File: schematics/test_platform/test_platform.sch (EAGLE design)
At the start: 13 parts

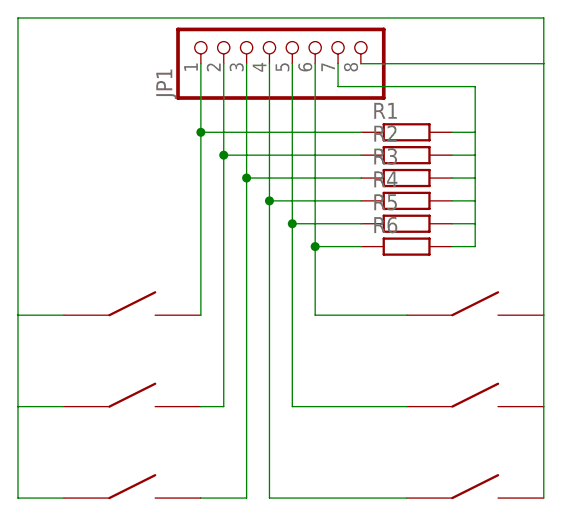
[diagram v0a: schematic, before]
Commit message: test platform ready for production, except for button footprints
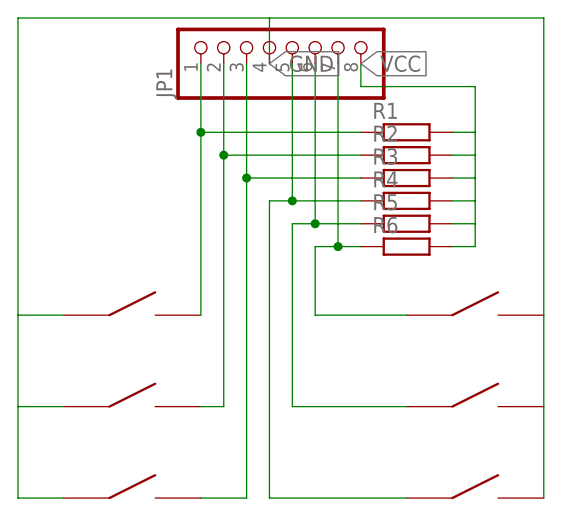
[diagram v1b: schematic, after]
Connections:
- removed net N$7: JP1.7, R1.2, R2.2, R3.2, R4.2, R5.2, R6.2
- removed net N$8: JP1.8, U$1.A, U$2.A, U$3.A, U$4.B, U$5.B, U$6.B
- new net GND: JP1.4, U$1.A, U$2.A, U$3.A, U$4.B, U$5.B, U$6.B
- new net VCC: JP1.8, R1.2, R2.2, R3.2, R4.2, R5.2, R6.2
- net N$4: now also JP1.5; no longer JP1.4
- net N$5: now also JP1.6; no longer JP1.5
- net N$6: now also JP1.7; no longer JP1.6
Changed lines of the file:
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@@
 <net name="N$4" class="0">
 <segment>
-<pinref part="JP1" gate="G$1" pin="4"/>
-<wire x1="73.66" y1="76.2" x2="73.66" y2="60.96" width="0.1524" layer="91"/>
 <pinref part="U$6" gate="G$1" pin="A"/>
 <wire x1="73.66" y1="60.96" x2="73.66" y2="27.94" width="0.1524" layer="91"/>
 <wire x1="73.66" y1="27.94" x2="88.9" y2="27.94" width="0.1524" layer="91"/>
 <pinref part="R4" gate="G$1" pin="1"/>
-<wire x1="73.66" y1="60.96" x2="83.82" y2="60.96" width="0.1524" layer="91"/>
-<junction x="73.66" y="60.96"/>
+<wire x1="73.66" y1="60.96" x2="76.2" y2="60.96" width="0.1524" layer="91"/>
+<pinref part="JP1" gate="G$1" pin="5"/>
+<wire x1="76.2" y1="60.96" x2="83.82" y2="60.96" width="0.1524" layer="91"/>
+<wire x1="76.2" y1="76.2" x2="76.2" y2="60.96" width="0.1524" layer="91"/>
+<junction x="76.2" y="60.96"/>
 </segment>
 </net>
@@
 <pinref part="U$5" gate="G$1" pin="A"/>
 <wire x1="88.9" y1="38.1" x2="76.2" y2="38.1" width="0.1524" layer="91"/>
-<pinref part="JP1" gate="G$1" pin="5"/>
 <wire x1="76.2" y1="38.1" x2="76.2" y2="58.42" width="0.1524" layer="91"/>
 <pinref part="R5" gate="G$1" pin="1"/>
-<wire x1="76.2" y1="58.42" x2="76.2" y2="76.2" width="0.1524" layer="91"/>
-<wire x1="83.82" y1="58.42" x2="76.2" y2="58.42" width="0.1524" layer="91"/>
-<junction x="76.2" y="58.42"/>
+<wire x1="83.82" y1="58.42" x2="78.74" y2="58.42" width="0.1524" layer="91"/>
+<pinref part="JP1" gate="G$1" pin="6"/>
+<wire x1="78.74" y1="58.42" x2="76.2" y2="58.42" width="0.1524" layer="91"/>
+<wire x1="78.74" y1="76.2" x2="78.74" y2="58.42" width="0.1524" layer="91"/>
+<junction x="78.74" y="58.42"/>
 </segment>
 </net>
 <net name="N$6" class="0">
 <segment>
-<pinref part="JP1" gate="G$1" pin="6"/>
-<wire x1="78.74" y1="76.2" x2="78.74" y2="55.88" width="0.1524" layer="91"/>
 <pinref part="U$4" gate="G$1" pin="A"/>
 <wire x1="78.74" y1="55.88" x2="78.74" y2="48.26" width="0.1524" layer="91"/>
 <wire x1="78.74" y1="48.26" x2="88.9" y2="48.26" width="0.1524" layer="91"/>
 <pinref part="R6" gate="G$1" pin="1"/>
-<wire x1="78.74" y1="55.88" x2="83.82" y2="55.88" width="0.1524" layer="91"/>
-<junction x="78.74" y="55.88"/>
+<wire x1="78.74" y1="55.88" x2="81.28" y2="55.88" width="0.1524" layer="91"/>
+<pinref part="JP1" gate="G$1" pin="7"/>
+<wire x1="81.28" y1="55.88" x2="83.82" y2="55.88" width="0.1524" layer="91"/>
+<wire x1="81.28" y1="76.2" x2="81.28" y2="55.88" width="0.1524" layer="91"/>
+<junction x="81.28" y="55.88"/>
 </segment>
 </net>
-<net name="N$8" class="0">
+<net name="GND" class="0">
 <segment>
 <pinref part="U$6" gate="G$1" pin="B"/>
@@
 <wire x1="104.14" y1="38.1" x2="104.14" y2="48.26" width="0.1524" layer="91"/>
 <pinref part="U$4" gate="G$1" pin="B"/>
-<wire x1="104.14" y1="48.26" x2="104.14" y2="76.2" width="0.1524" layer="91"/>
+<wire x1="104.14" y1="48.26" x2="104.14" y2="81.28" width="0.1524" layer="91"/>
 <pinref part="U$3" gate="G$1" pin="A"/>
-<wire x1="104.14" y1="76.2" x2="104.14" y2="81.28" width="0.1524" layer="91"/>
 <wire x1="50.8" y1="27.94" x2="45.72" y2="27.94" width="0.1524" layer="91"/>
 <wire x1="45.72" y1="27.94" x2="45.72" y2="38.1" width="0.1524" layer="91"/>
 <wire x1="45.72" y1="38.1" x2="45.72" y2="48.26" width="0.1524" layer="91"/>
 <wire x1="45.72" y1="48.26" x2="45.72" y2="81.28" width="0.1524" layer="91"/>
-<wire x1="45.72" y1="81.28" x2="104.14" y2="81.28" width="0.1524" layer="91"/>
+<wire x1="45.72" y1="81.28" x2="73.66" y2="81.28" width="0.1524" layer="91"/>
 <pinref part="U$1" gate="G$1" pin="A"/>
+<wire x1="73.66" y1="81.28" x2="104.14" y2="81.28" width="0.1524" layer="91"/>
 <wire x1="50.8" y1="48.26" x2="45.72" y2="48.26" width="0.1524" layer="91"/>
 <pinref part="U$2" gate="G$1" pin="A"/>
 <wire x1="50.8" y1="38.1" x2="45.72" y2="38.1" width="0.1524" layer="91"/>
-<pinref part="JP1" gate="G$1" pin="8"/>
-<wire x1="83.82" y1="76.2" x2="104.14" y2="76.2" width="0.1524" layer="91"/>
+<pinref part="JP1" gate="G$1" pin="4"/>
+<wire x1="73.66" y1="76.2" x2="73.66" y2="81.28" width="0.1524" layer="91"/>
+<label x="73.66" y="76.2" size="1.778" layer="95" xref="yes"/>
 </segment>
 </net>
-<net name="N$7" class="0">
+<net name="VCC" class="0">
 <segment>
-<pinref part="JP1" gate="G$1" pin="7"/>
-<wire x1="81.28" y1="76.2" x2="81.28" y2="73.66" width="0.1524" layer="91"/>
-<wire x1="81.28" y1="73.66" x2="96.52" y2="73.66" width="0.1524" layer="91"/>
 <wire x1="96.52" y1="73.66" x2="96.52" y2="68.58" width="0.1524" layer="91"/>
 <pinref part="R6" gate="G$1" pin="2"/>
@@
 <pinref part="R1" gate="G$1" pin="2"/>
 <wire x1="93.98" y1="68.58" x2="96.52" y2="68.58" width="0.1524" layer="91"/>
+<pinref part="JP1" gate="G$1" pin="8"/>
+<wire x1="96.52" y1="73.66" x2="83.82" y2="73.66" width="0.1524" layer="91"/>
+<wire x1="83.82" y1="73.66" x2="83.82" y2="76.2" width="0.1524" layer="91"/>
+<label x="83.82" y="76.2" size="1.778" layer="95" xref="yes"/>
 </segment>
 </net>

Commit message: circuit for testplatform done
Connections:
- net N$4: now also U$4.A; no longer U$6.A
- net N$6: now also U$6.A; no longer U$4.A
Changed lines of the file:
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@@
 <parts>
 <part name="JP1" library="adafruit" deviceset="PINHD-1X8" device="BIG"/>
+<part name="R1" library="rcl" deviceset="R-EU_" device="M0805"/>
+<part name="R2" library="rcl" deviceset="R-EU_" device="M0805"/>
+<part name="R3" library="rcl" deviceset="R-EU_" device="M0805"/>
+<part name="R4" library="rcl" deviceset="R-EU_" device="M0805"/>
+<part name="R6" library="rcl" deviceset="R-EU_" device="M0805"/>
+<part name="R5" library="rcl" deviceset="R-EU_" device="M0805"/>
 <part name="U$1" library="BraillePad" deviceset="SMT_BUTTON" device=""/>
 <part name="U$2" library="BraillePad" deviceset="SMT_BUTTON" device=""/>
@@
 <part name="U$5" library="BraillePad" deviceset="SMT_BUTTON" device=""/>
 <part name="U$6" library="BraillePad" deviceset="SMT_BUTTON" device=""/>
-<part name="R1" library="rcl" deviceset="R-EU_" device="M0805"/>
-<part name="R2" library="rcl" deviceset="R-EU_" device="M0805"/>
-<part name="R3" library="rcl" deviceset="R-EU_" device="M0805"/>
-<part name="R4" library="rcl" deviceset="R-EU_" device="M0805"/>
-<part name="R6" library="rcl" deviceset="R-EU_" device="M0805"/>
-<part name="R5" library="rcl" deviceset="R-EU_" device="M0805"/>
 </parts>
 <sheets>
@@
 <instances>
 <instance part="JP1" gate="G$1" x="73.66" y="78.74" rot="R90"/>
-<instance part="U$1" gate="G$1" x="58.42" y="48.26"/>
-<instance part="U$2" gate="G$1" x="58.42" y="38.1"/>
-<instance part="U$3" gate="G$1" x="58.42" y="27.94"/>
-<instance part="U$4" gate="G$1" x="96.52" y="48.26"/>
-<instance part="U$5" gate="G$1" x="96.52" y="38.1"/>
-<instance part="U$6" gate="G$1" x="96.52" y="27.94"/>
 <instance part="R1" gate="G$1" x="88.9" y="68.58"/>
 <instance part="R2" gate="G$1" x="88.9" y="66.04"/>
@@
 <instance part="R6" gate="G$1" x="88.9" y="55.88"/>
 <instance part="R5" gate="G$1" x="88.9" y="58.42"/>
+<instance part="U$1" gate="G$1" x="58.42" y="48.26"/>
+<instance part="U$2" gate="G$1" x="58.42" y="38.1"/>
+<instance part="U$3" gate="G$1" x="58.42" y="27.94"/>
+<instance part="U$4" gate="G$1" x="96.52" y="27.94"/>
+<instance part="U$5" gate="G$1" x="96.52" y="38.1"/>
+<instance part="U$6" gate="G$1" x="96.52" y="48.26"/>
 </instances>
 <busses>
@@
 <pinref part="JP1" gate="G$1" pin="1"/>
 <wire x1="66.04" y1="76.2" x2="66.04" y2="68.58" width="0.1524" layer="91"/>
-<pinref part="U$1" gate="G$1" pin="B"/>
 <pinref part="R1" gate="G$1" pin="1"/>
 <wire x1="66.04" y1="68.58" x2="66.04" y2="48.26" width="0.1524" layer="91"/>
 <wire x1="83.82" y1="68.58" x2="66.04" y2="68.58" width="0.1524" layer="91"/>
 <junction x="66.04" y="68.58"/>
+<pinref part="U$1" gate="G$1" pin="B"/>
 </segment>
 </net>
@@
 <pinref part="JP1" gate="G$1" pin="2"/>
 <wire x1="68.58" y1="76.2" x2="68.58" y2="66.04" width="0.1524" layer="91"/>
-<pinref part="U$2" gate="G$1" pin="B"/>
 <wire x1="68.58" y1="66.04" x2="68.58" y2="38.1" width="0.1524" layer="91"/>
 <wire x1="66.04" y1="38.1" x2="68.58" y2="38.1" width="0.1524" layer="91"/>
@@
 <wire x1="68.58" y1="66.04" x2="83.82" y2="66.04" width="0.1524" layer="91"/>
 <junction x="68.58" y="66.04"/>
+<pinref part="U$2" gate="G$1" pin="B"/>
 </segment>
 </net>
@@
 <pinref part="JP1" gate="G$1" pin="3"/>
 <wire x1="71.12" y1="76.2" x2="71.12" y2="63.5" width="0.1524" layer="91"/>
-<pinref part="U$3" gate="G$1" pin="B"/>
 <wire x1="71.12" y1="63.5" x2="71.12" y2="27.94" width="0.1524" layer="91"/>
 <wire x1="66.04" y1="27.94" x2="71.12" y2="27.94" width="0.1524" layer="91"/>
@@
 <wire x1="83.82" y1="63.5" x2="71.12" y2="63.5" width="0.1524" layer="91"/>
 <junction x="71.12" y="63.5"/>
+<pinref part="U$3" gate="G$1" pin="B"/>
 </segment>
 </net>
 <net name="N$4" class="0">
 <segment>
-<pinref part="U$6" gate="G$1" pin="A"/>
 <wire x1="73.66" y1="60.96" x2="73.66" y2="27.94" width="0.1524" layer="91"/>
 <wire x1="73.66" y1="27.94" x2="88.9" y2="27.94" width="0.1524" layer="91"/>
@@
 <wire x1="76.2" y1="76.2" x2="76.2" y2="60.96" width="0.1524" layer="91"/>
 <junction x="76.2" y="60.96"/>
+<pinref part="U$4" gate="G$1" pin="A"/>
 </segment>
 </net>
 <net name="N$5" class="0">
 <segment>
-<pinref part="U$5" gate="G$1" pin="A"/>
 <wire x1="88.9" y1="38.1" x2="76.2" y2="38.1" width="0.1524" layer="91"/>
 <wire x1="76.2" y1="38.1" x2="76.2" y2="58.42" width="0.1524" layer="91"/>
@@
 <wire x1="78.74" y1="76.2" x2="78.74" y2="58.42" width="0.1524" layer="91"/>
 <junction x="78.74" y="58.42"/>
+<pinref part="U$5" gate="G$1" pin="A"/>
 </segment>
 </net>
 <net name="N$6" class="0">
 <segment>
-<pinref part="U$4" gate="G$1" pin="A"/>
 <wire x1="78.74" y1="55.88" x2="78.74" y2="48.26" width="0.1524" layer="91"/>
 <wire x1="78.74" y1="48.26" x2="88.9" y2="48.26" width="0.1524" layer="91"/>
@@
 <wire x1="81.28" y1="76.2" x2="81.28" y2="55.88" width="0.1524" layer="91"/>
 <junction x="81.28" y="55.88"/>
+<pinref part="U$6" gate="G$1" pin="A"/>
 </segment>
 </net>
 <net name="GND" class="0">
 <segment>
-<pinref part="U$6" gate="G$1" pin="B"/>
 <wire x1="104.14" y1="27.94" x2="104.14" y2="38.1" width="0.1524" layer="91"/>
-<pinref part="U$5" gate="G$1" pin="B"/>
 <wire x1="104.14" y1="38.1" x2="104.14" y2="48.26" width="0.1524" layer="91"/>
-<pinref part="U$4" gate="G$1" pin="B"/>
 <wire x1="104.14" y1="48.26" x2="104.14" y2="81.28" width="0.1524" layer="91"/>
-<pinref part="U$3" gate="G$1" pin="A"/>
 <wire x1="50.8" y1="27.94" x2="45.72" y2="27.94" width="0.1524" layer="91"/>
 <wire x1="45.72" y1="27.94" x2="45.72" y2="38.1" width="0.1524" layer="91"/>
@@
 <wire x1="45.72" y1="48.26" x2="45.72" y2="81.28" width="0.1524" layer="91"/>
 <wire x1="45.72" y1="81.28" x2="73.66" y2="81.28" width="0.1524" layer="91"/>
-<pinref part="U$1" gate="G$1" pin="A"/>
 <wire x1="73.66" y1="81.28" x2="104.14" y2="81.28" width="0.1524" layer="91"/>
 <wire x1="50.8" y1="48.26" x2="45.72" y2="48.26" width="0.1524" layer="91"/>
-<pinref part="U$2" gate="G$1" pin="A"/>
 <wire x1="50.8" y1="38.1" x2="45.72" y2="38.1" width="0.1524" layer="91"/>
 <pinref part="JP1" gate="G$1" pin="4"/>
 <wire x1="73.66" y1="76.2" x2="73.66" y2="81.28" width="0.1524" layer="91"/>
 <label x="73.66" y="76.2" size="1.778" layer="95" xref="yes"/>
+<pinref part="U$1" gate="G$1" pin="A"/>
+<pinref part="U$2" gate="G$1" pin="A"/>
+<pinref part="U$3" gate="G$1" pin="A"/>
+<pinref part="U$4" gate="G$1" pin="B"/>
+<pinref part="U$5" gate="G$1" pin="B"/>
+<junction x="104.14" y="38.1"/>
+<pinref part="U$6" gate="G$1" pin="B"/>
+<junction x="104.14" y="48.26"/>
 </segment>
 </net>
